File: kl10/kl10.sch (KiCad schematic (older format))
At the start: 0 parts

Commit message: checkpoint
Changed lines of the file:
@@
 $Descr B 17000 11000
 encoding utf-8
-Sheet 1 3
-Title "KL10-PV Based System"
+Sheet 1 4
+Title "DATA PATH ARX & MQ Registers"
 Date "3/6/1980"
 Rev "C"
 Comp "Digitized Equipment Corporation"
-Comment1 "KL10-PV-4"
+Comment1 "M8512-0-DP02"
 Comment2 ""
 Comment3 ""
@@
 F0 "dpa02" 60
 F1 "dpa02.sch" 60
-F2 "arxm" I L 8950 4800 60
-F3 "ad" I L 8950 4900 60
-F4 "mq" I L 8950 5000 60
-F5 "sh" I L 8950 5100 60
-F6 "adx" I L 8950 5200 60
-F7 "cache-data" I L 8950 4400 60
-F8 "mqm" O R 9950 3350 60
-F9 "dp04-clk" I L 8950 3350 60
-F10 "ctl-arx-load" I L 8950 3600 60
-F11 "arxm.0-d7" I L 8950 4050 60
-F12 "arxm-sel-1" I L 8950 3900 60
-F13 "arxm-sel-2" I L 8950 3800 60
-F14 "arxm-sel-4" I L 8950 3700 60
-F15 "arxm.1-d7" I L 8950 4150 60
-F16 "arxm.5-d5" I L 8950 4250 60
-F17 "ctl-mqm-en" I L 8950 4700 60
-F18 "ctl-mqm-sel-2" I L 8950 4600 60
-F19 "ctl-mqm-sel-1" I L 8950 4500 60
-F20 "mqm.0-d10" I L 8950 5450 60
-F21 "mqm.0-d00" I L 8950 5350 60
-F22 "ctl-mq-sel-1" I L 8950 5600 60
-F23 "ctl-mq-sel-2" I L 8950 5700 60
-F24 "mqm.3-5-dr" I L 8950 5850 60
+F2 "ad" I L 8950 4900 60
+F3 "sh" I L 8950 5100 60
+F4 "adx" I L 8950 5200 60
+F5 "cache-data" I L 8950 4400 60
+F6 "mqm" O R 9950 3850 60
+F7 "dp04-clk" I L 8950 3350 60
+F8 "ctl-arx-load" I L 8950 3600 60
+F9 "arxm.0-d7" I L 8950 4050 60
+F10 "arxm-sel-1" I L 8950 3900 60
+F11 "arxm-sel-2" I L 8950 3800 60
+F12 "arxm-sel-4" I L 8950 3700 60
+F13 "arxm.1-d7" I L 8950 4150 60
+F14 "arxm.5-d5" I L 8950 4250 60
+F15 "ctl-mqm-en" I L 8950 4700 60
+F16 "ctl-mqm-sel-2" I L 8950 4600 60
+F17 "ctl-mqm-sel-1" I L 8950 4500 60
+F18 "mqm.0-d10" I L 8950 5450 60
+F19 "mqm.0-d00" I L 8950 5350 60
+F20 "ctl-mq-sel-1" I L 8950 5600 60
+F21 "ctl-mq-sel-2" I L 8950 5700 60
+F22 "mqm.3-5-dr" I L 8950 5850 60
+F23 "arxm" O R 9950 3450 60
+F24 "arx" O R 9950 3350 60
+F25 "mq" O R 9950 3750 60
+$EndSheet
+$Sheet
+S 10150 3250 1100 2850
+U 57ACBE4E
+F0 "dpa03" 60
+F1 "dpa03.sch" 60
+F2 "ad-ex" O R 11250 3450 60
+F3 "ad" O R 11250 3350 60
+F4 "fm" I L 10150 4000 60
+F5 "br" I L 10150 3550 60
+F6 "arx" I L 10150 3450 60
+F7 "mq" I L 10150 3800 60
+F8 "pc" I L 10150 3900 60
+F9 "brx" I L 10150 3650 60
+F10 "ar" I L 10150 3350 60
+F11 "vma-held-or-pc" I L 10150 4700 60
 $EndSheet
 $EndSCHEMATC

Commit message: checkpoint
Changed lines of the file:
@@
 $Descr B 17000 11000
 encoding utf-8
-Sheet 1 4
-Title "DATA PATH ARX & MQ Registers"
-Date "3/6/1980"
-Rev "C"
+Sheet 1 6
+Title "KL10-PV CPU"
+Date ""
+Rev "A"
 Comp "Digitized Equipment Corporation"
-Comment1 "M8512-0-DP02"
+Comment1 ""
 Comment2 ""
 Comment3 ""
@@
 NoConn ~ 9350 -100
 $Sheet
-S 7850 3250 800  2100
-U 57A8973E
-F0 "dpa01" 60
-F1 "dpa01.sch" 60
-F2 "ar-0-2-sel" I L 7850 3600 60
-F3 "dp04-clk" I L 7850 3350 60
-F4 "ar-3-5-sel" I L 7850 3700 60
-F5 "arm-sel-4" I L 7850 4200 60
-F6 "arm-sel-2" I L 7850 4100 60
-F7 "arm-sel-1" I L 7850 4000 60
-F8 "arm-en" I L 7850 3900 60
-F9 "ar" O R 8650 3350 60
-F10 "arm.5-x5" I L 7850 4650 60
-F11 "arm.1-x7" I L 7850 4400 60
-F12 "arm.0-x7" I L 7850 4300 60
-F13 "arm.4-x5" I L 7850 4550 60
-F14 "armm" I L 7850 5200 60
-F15 "ad" I L 7850 5100 60
-F16 "cache-data" I L 7850 4800 60
-F17 "ebus-d" I L 7850 4900 60
-F18 "sh" I L 7850 5300 60
-$EndSheet
-$Sheet
-S 8950 3250 1000 2850
-U 57AC9C69
-F0 "dpa02" 60
-F1 "dpa02.sch" 60
-F2 "ad" I L 8950 4900 60
-F3 "sh" I L 8950 5100 60
-F4 "adx" I L 8950 5200 60
-F5 "cache-data" I L 8950 4400 60
-F6 "mqm" O R 9950 3850 60
-F7 "dp04-clk" I L 8950 3350 60
-F8 "ctl-arx-load" I L 8950 3600 60
-F9 "arxm.0-d7" I L 8950 4050 60
-F10 "arxm-sel-1" I L 8950 3900 60
-F11 "arxm-sel-2" I L 8950 3800 60
-F12 "arxm-sel-4" I L 8950 3700 60
-F13 "arxm.1-d7" I L 8950 4150 60
-F14 "arxm.5-d5" I L 8950 4250 60
-F15 "ctl-mqm-en" I L 8950 4700 60
-F16 "ctl-mqm-sel-2" I L 8950 4600 60
-F17 "ctl-mqm-sel-1" I L 8950 4500 60
-F18 "mqm.0-d10" I L 8950 5450 60
-F19 "mqm.0-d00" I L 8950 5350 60
-F20 "ctl-mq-sel-1" I L 8950 5600 60
-F21 "ctl-mq-sel-2" I L 8950 5700 60
-F22 "mqm.3-5-dr" I L 8950 5850 60
-F23 "arxm" O R 9950 3450 60
-F24 "arx" O R 9950 3350 60
-F25 "mq" O R 9950 3750 60
-$EndSheet
-$Sheet
-S 10150 3250 1100 2850
-U 57ACBE4E
-F0 "dpa03" 60
-F1 "dpa03.sch" 60
-F2 "ad-ex" O R 11250 3450 60
-F3 "ad" O R 11250 3350 60
-F4 "fm" I L 10150 4000 60
-F5 "br" I L 10150 3550 60
-F6 "arx" I L 10150 3450 60
-F7 "mq" I L 10150 3800 60
-F8 "pc" I L 10150 3900 60
-F9 "brx" I L 10150 3650 60
-F10 "ar" I L 10150 3350 60
-F11 "vma-held-or-pc" I L 10150 4700 60
+S 4250 3400 1000 3050
+U 57B68864
+F0 "dpa" 60
+F1 "dpa.sch" 60
 $EndSheet
 $EndSCHEMATC

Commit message: checkpoint
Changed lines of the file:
@@
 encoding utf-8
 Sheet 1 6
-Title "KL10-PV CPU"
-Date ""
-Rev "A"
+Title "KL10-PV BASED SYSTEM"
+Date "6/3/1980"
+Rev "C"
 Comp "Digitized Equipment Corporation"
-Comment1 ""
+Comment1 "KL10-PV-4"
 Comment2 ""
 Comment3 ""
@@
 NoConn ~ 9350 -100
 $Sheet
-S 4250 3400 1000 3050
+S 1550 1200 700  1250
 U 57B68864
-F0 "dpa" 60
+F0 "dpa.0" 60
 F1 "dpa.sch" 60
+F2 "ar" O R 2250 1300 60
+F3 "arx" O R 2250 1400 60
+F4 "arxm" O R 2250 1700 60
+F5 "mq" O R 2250 1850 60
+F6 "mqm" O R 2250 1950 60
+F7 "br" I L 1550 1450 60
+F8 "brx" I L 1550 1550 60
+F9 "fm" I L 1550 2050 60
+F10 "ad" I L 1550 1700 60
+F11 "armm" I L 1550 2250 60
+F12 "sh" I L 1550 2150 60
+F13 "adx" I L 1550 1800 60
+F14 "ad-ex" O R 2250 1550 60
 $EndSheet
 $EndSCHEMATC

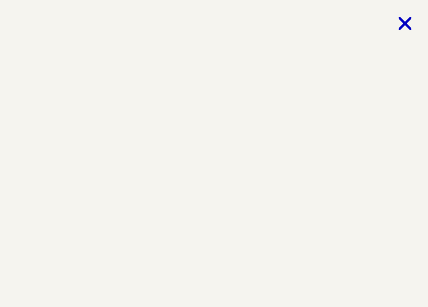
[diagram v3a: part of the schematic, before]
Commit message: Update to kicad 5.1.2
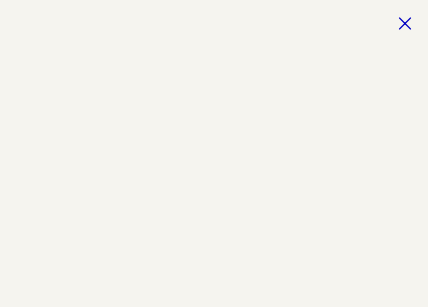
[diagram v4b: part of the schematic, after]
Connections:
- no-connect marks 8 -> 1
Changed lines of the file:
@@
-EESchema Schematic File Version 2
-LIBS:o_ecl
-LIBS:ecl
-LIBS:power
-LIBS:device
-LIBS:transistors
-LIBS:conn
-LIBS:linear
-LIBS:regul
-LIBS:74xx
-LIBS:cmos4000
-LIBS:adc-dac
-LIBS:memory
-LIBS:xilinx
-LIBS:microcontrollers
-LIBS:dsp
-LIBS:microchip
-LIBS:analog_switches
-LIBS:motorola
-LIBS:texas
-LIBS:intel
-LIBS:audio
-LIBS:interface
-LIBS:digital-audio
-LIBS:philips
-LIBS:display
-LIBS:cypress
-LIBS:siliconi
-LIBS:opto
-LIBS:atmel
-LIBS:contrib
-LIBS:valves
+EESchema Schematic File Version 4
 LIBS:kl10-cache
-EELAYER 25 0
+EELAYER 30 0
 EELAYER END
 $Descr B 17000 11000
@@
 $EndDescr
 NoConn ~ 9350 -100
-NoConn ~ 9350 -100
-NoConn ~ 9350 -100
-NoConn ~ 9350 -100
-NoConn ~ 9350 -100
-NoConn ~ 9350 -100
-NoConn ~ 9350 -100
-NoConn ~ 9350 -100
 $Sheet
